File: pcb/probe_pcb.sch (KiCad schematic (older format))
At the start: 42 parts

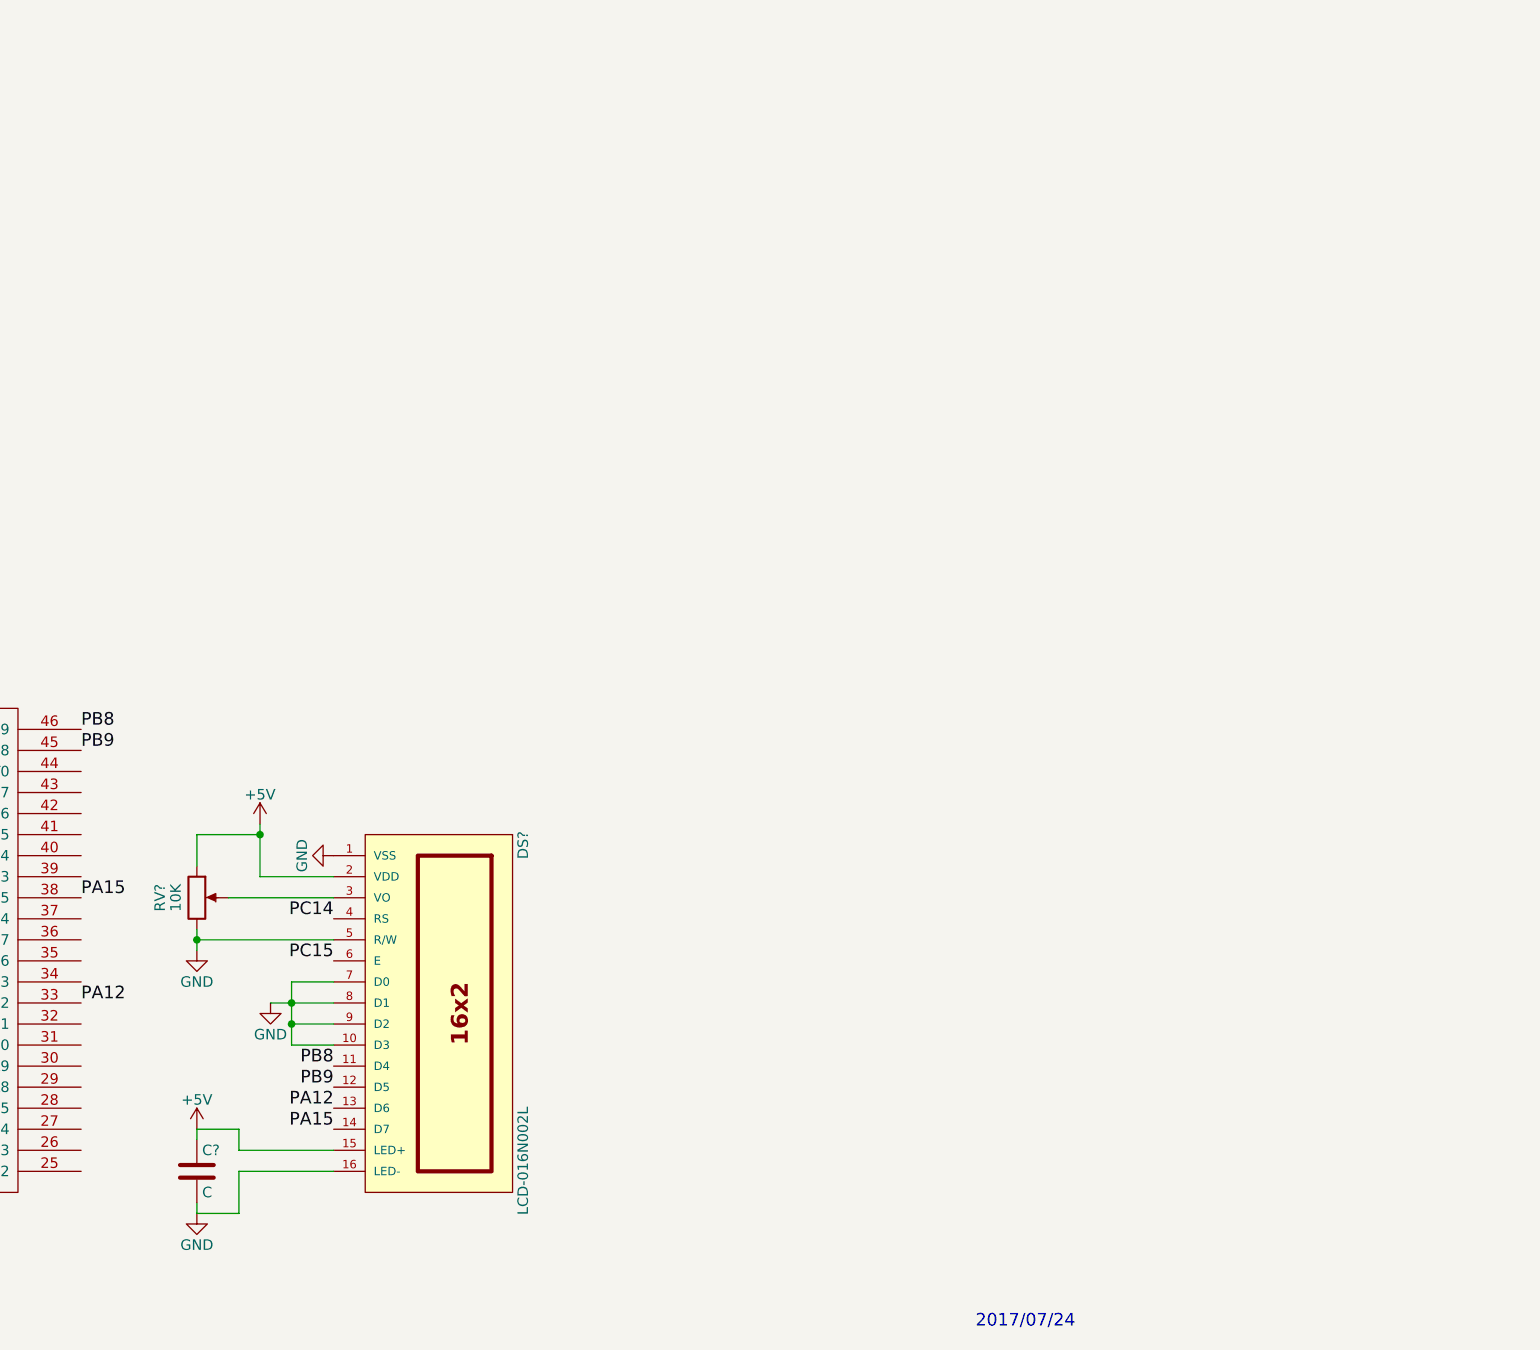
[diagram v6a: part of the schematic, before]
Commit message: Added ribbon cable connector for Pi, pi LCD
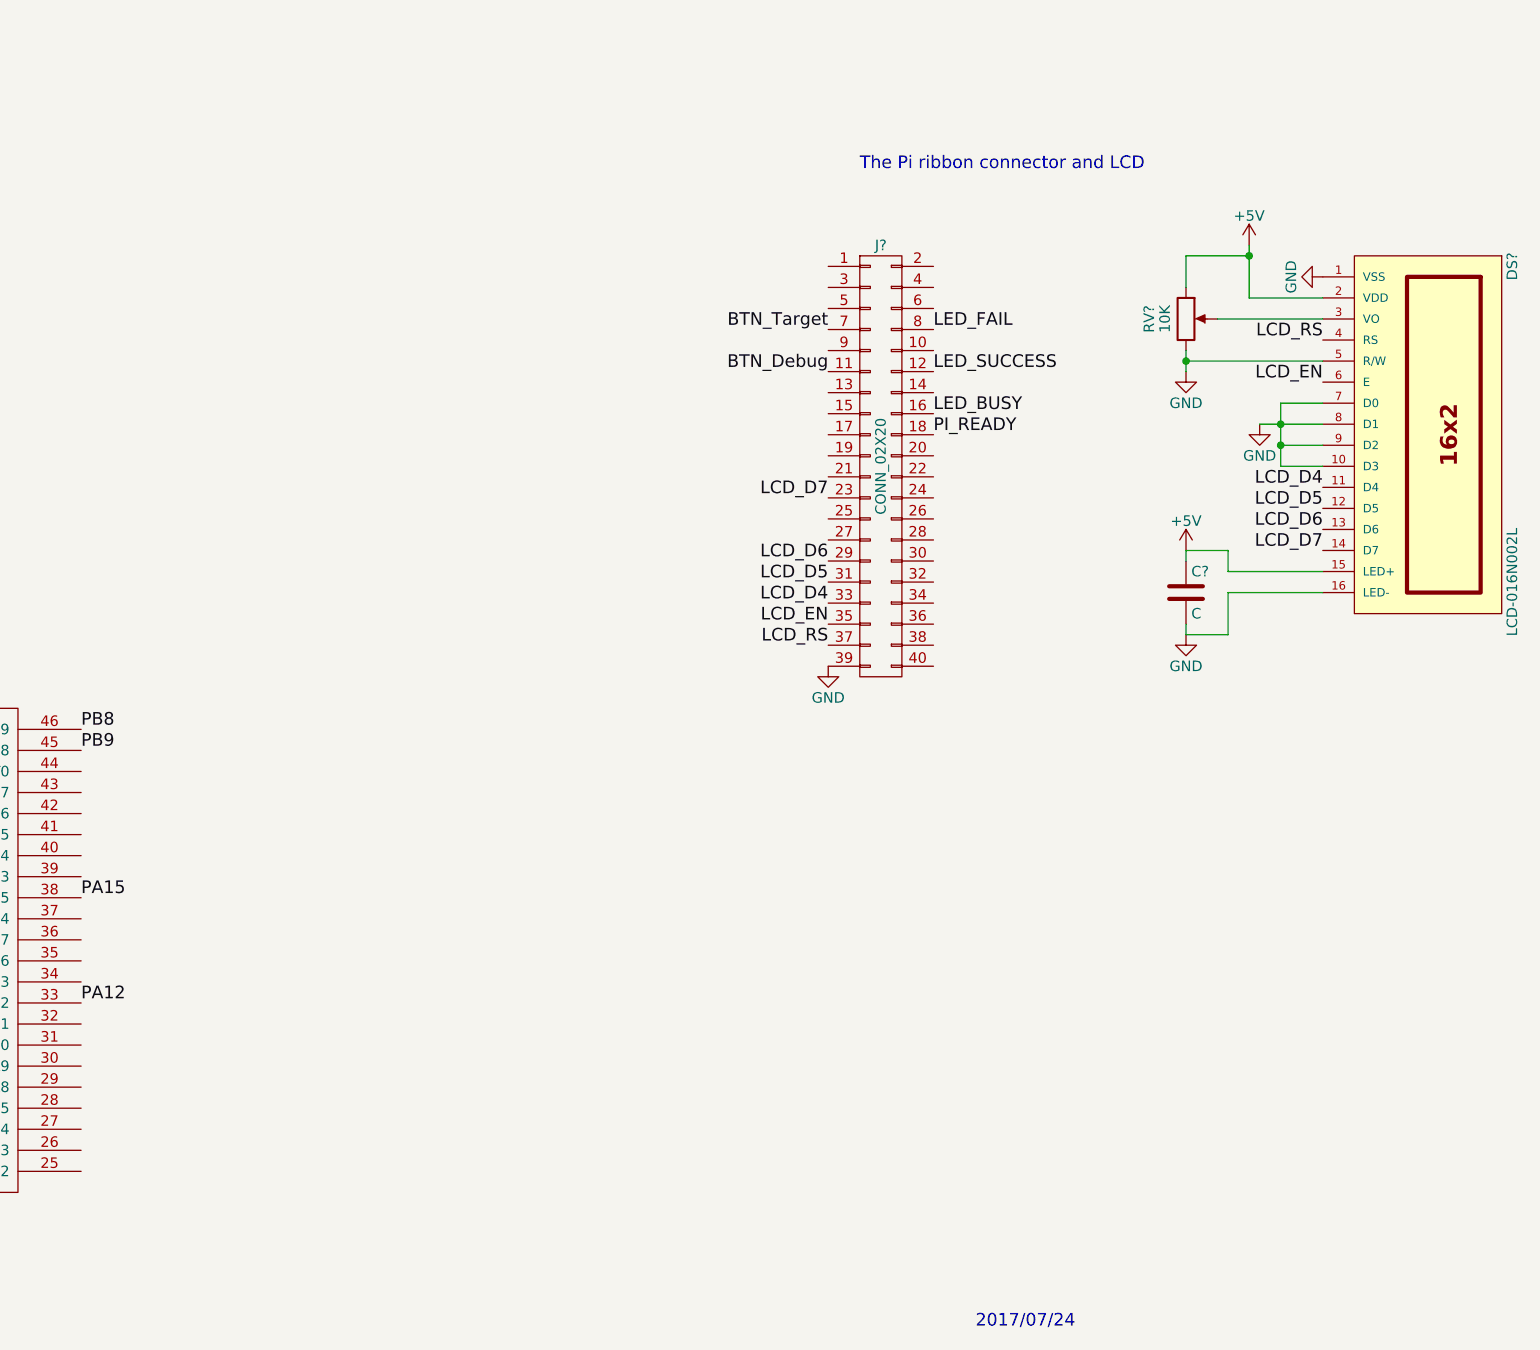
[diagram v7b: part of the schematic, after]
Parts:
- added J?: CONN_02X20, symbol CONN_02X20
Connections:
- net BTN_Debug: now also J?.11 (P11)
- net BTN_Target: now also J?.7 (P7)
- net GND: now also J?.39 (P39)
- net LED_BUSY: now also J?.16 (P16)
- net LED_FAIL: now also J?.8 (P8)
- net LED_SUCCESS: now also J?.12 (P12)
- net PA12: no longer DS?.13 (D6)
- net PA15: no longer DS?.14 (D7)
- net PB8: no longer DS?.11 (D4)
- net PB9: no longer DS?.12 (D5)
- net PC14: no longer DS?.4 (RS)
- net PC15: no longer DS?.6 (E)
- net PI_READY: now also J?.18 (P18)
- new net LCD_D4: DS?.11 (D4), J?.33 (P33)
- new net LCD_D5: DS?.12 (D5), J?.31 (P31)
- new net LCD_D6: DS?.13 (D6), J?.29 (P29)
- new net LCD_D7: DS?.14 (D7), J?.23 (P23)
- new net LCD_EN: DS?.6 (E), J?.35 (P35)
- new net LCD_RS: DS?.4 (RS), J?.37 (P37)
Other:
- note added: "The Pi ribbon connector and LCD"
- moved on the sheet: C?, DS?, RV?
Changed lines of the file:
@@
 LIBS:valves
 LIBS:stm_jig_lib
+LIBS:raspberrypi-gpio-cache
 LIBS:probe_pcb-cache
 EELAYER 25 0
@@
 L LCD-016N002L DS?
 U 1 1 5975A4A1
-P 10500 9550
-F 0 "DS?" H 9700 9950 50  0000 C CNN
-F 1 "LCD-016N002L" H 11200 9950 50  0000 C CNN
-F 2 "WC1602A" H 10500 9500 50  0001 C CIN
-F 3 "" H 10500 9550 50  0001 C CNN
-	1    10500 9550
+P 15200 6800
+F 0 "DS?" H 14400 7200 50  0000 C CNN
+F 1 "LCD-016N002L" H 15900 7200 50  0000 C CNN
+F 2 "WC1602A" H 15200 6750 50  0001 C CIN
+F 3 "" H 15200 6800 50  0001 C CNN
+	1    15200 6800
 	0    1    1    0
 $EndComp
@@
 Text Label 6900 8550 2    60   ~ 0
 PC15
-Text Label 10000 9100 2    60   ~ 0
-PC14
-Text Label 10000 9300 2    60   ~ 0
-PC15
 Text Label 8800 8200 0    60   ~ 0
 PB8
 Text Label 8800 8300 0    60   ~ 0
-PB9
-Text Label 10000 9800 2    60   ~ 0
-PB8
-Text Label 10000 9900 2    60   ~ 0
 PB9
 Text Label 8800 9500 0    60   ~ 0
@@
 Text Label 8800 9000 0    60   ~ 0
 PA15
-Text Label 10000 10100 2    60   ~ 0
-PA15
-Text Label 10000 10000 2    60   ~ 0
-PA12
-Wire Wire Line
-	10000 8900 9650 8900
-Wire Wire Line
-	9650 8900 9650 8650
+Wire Wire Line
+	14700 6150 14350 6150
+Wire Wire Line
+	14350 6150 14350 5900
 $Comp
 L +5V #PWR?
 U 1 1 59761C03
-P 9650 8650
-F 0 "#PWR?" H 9650 8500 50  0001 C CNN
-F 1 "+5V" H 9650 8790 50  0000 C CNN
-F 2 "" H 9650 8650 50  0001 C CNN
-F 3 "" H 9650 8650 50  0001 C CNN
-	1    9650 8650
+P 14350 5900
+F 0 "#PWR?" H 14350 5750 50  0001 C CNN
+F 1 "+5V" H 14350 6040 50  0000 C CNN
+F 2 "" H 14350 5900 50  0001 C CNN
+F 3 "" H 14350 5900 50  0001 C CNN
+	1    14350 5900
 	1    0    0    -1
 $EndComp
@@
 L POT RV?
 U 1 1 59761CDF
-P 9350 9000
-F 0 "RV?" V 9175 9000 50  0000 C CNN
-F 1 "10K" V 9250 9000 50  0000 C CNN
-F 2 "" H 9350 9000 50  0001 C CNN
-F 3 "" H 9350 9000 50  0001 C CNN
-	1    9350 9000
-	1    0    0    -1
-$EndComp
-Wire Wire Line
-	9500 9000 10000 9000
-Wire Wire Line
-	9350 8850 9350 8700
-Wire Wire Line
-	9350 8700 9650 8700
-Connection ~ 9650 8700
+P 14050 6250
+F 0 "RV?" V 13875 6250 50  0000 C CNN
+F 1 "10K" V 13950 6250 50  0000 C CNN
+F 2 "" H 14050 6250 50  0001 C CNN
+F 3 "" H 14050 6250 50  0001 C CNN
+	1    14050 6250
+	1    0    0    -1
+$EndComp
+Wire Wire Line
+	14200 6250 14700 6250
+Wire Wire Line
+	14050 6100 14050 5950
+Wire Wire Line
+	14050 5950 14350 5950
+Connection ~ 14350 5950
 $Comp
 L GND #PWR?
 U 1 1 59761E45
-P 9350 9250
-F 0 "#PWR?" H 9350 9000 50  0001 C CNN
-F 1 "GND" H 9350 9100 50  0000 C CNN
-F 2 "" H 9350 9250 50  0001 C CNN
-F 3 "" H 9350 9250 50  0001 C CNN
-	1    9350 9250
-	1    0    0    -1
-$EndComp
-Wire Wire Line
-	9350 9150 9350 9250
-Wire Wire Line
-	10000 9200 9350 9200
-Connection ~ 9350 9200
+P 14050 6500
+F 0 "#PWR?" H 14050 6250 50  0001 C CNN
+F 1 "GND" H 14050 6350 50  0000 C CNN
+F 2 "" H 14050 6500 50  0001 C CNN
+F 3 "" H 14050 6500 50  0001 C CNN
+	1    14050 6500
+	1    0    0    -1
+$EndComp
+Wire Wire Line
+	14050 6400 14050 6500
+Wire Wire Line
+	14700 6450 14050 6450
+Connection ~ 14050 6450
 $Comp
 L GND #PWR?
 U 1 1 59761FC4
-P 10000 8800
-F 0 "#PWR?" H 10000 8550 50  0001 C CNN
-F 1 "GND" H 10000 8650 50  0000 C CNN
-F 2 "" H 10000 8800 50  0001 C CNN
-F 3 "" H 10000 8800 50  0001 C CNN
-	1    10000 8800
+P 14700 6050
+F 0 "#PWR?" H 14700 5800 50  0001 C CNN
+F 1 "GND" H 14700 5900 50  0000 C CNN
+F 2 "" H 14700 6050 50  0001 C CNN
+F 3 "" H 14700 6050 50  0001 C CNN
+	1    14700 6050
 	0    1    1    0
 $EndComp
@@
 L GND #PWR?
 U 1 1 59762012
-P 9700 9500
-F 0 "#PWR?" H 9700 9250 50  0001 C CNN
-F 1 "GND" H 9700 9350 50  0000 C CNN
-F 2 "" H 9700 9500 50  0001 C CNN
-F 3 "" H 9700 9500 50  0001 C CNN
-	1    9700 9500
-	1    0    0    -1
-$EndComp
-Wire Wire Line
-	9700 9500 10000 9500
-Wire Wire Line
-	10000 9600 9800 9600
-Wire Wire Line
-	9800 9400 9800 9700
-Connection ~ 9800 9500
-Wire Wire Line
-	9800 9700 10000 9700
-Connection ~ 9800 9600
-Wire Wire Line
-	10000 9400 9800 9400
+P 14400 6750
+F 0 "#PWR?" H 14400 6500 50  0001 C CNN
+F 1 "GND" H 14400 6600 50  0000 C CNN
+F 2 "" H 14400 6750 50  0001 C CNN
+F 3 "" H 14400 6750 50  0001 C CNN
+	1    14400 6750
+	1    0    0    -1
+$EndComp
+Wire Wire Line
+	14400 6750 14700 6750
+Wire Wire Line
+	14700 6850 14500 6850
+Wire Wire Line
+	14500 6650 14500 6950
+Connection ~ 14500 6750
+Wire Wire Line
+	14500 6950 14700 6950
+Connection ~ 14500 6850
+Wire Wire Line
+	14700 6650 14500 6650
 $Comp
 L GND #PWR?
 U 1 1 5976236D
-P 9350 10500
-F 0 "#PWR?" H 9350 10250 50  0001 C CNN
-F 1 "GND" H 9350 10350 50  0000 C CNN
-F 2 "" H 9350 10500 50  0001 C CNN
-F 3 "" H 9350 10500 50  0001 C CNN
-	1    9350 10500
+P 14050 7750
+F 0 "#PWR?" H 14050 7500 50  0001 C CNN
+F 1 "GND" H 14050 7600 50  0000 C CNN
+F 2 "" H 14050 7750 50  0001 C CNN
+F 3 "" H 14050 7750 50  0001 C CNN
+	1    14050 7750
 	1    0    0    -1
 $EndComp
@@
 L +5V #PWR?
 U 1 1 597623BB
-P 9350 10100
-F 0 "#PWR?" H 9350 9950 50  0001 C CNN
-F 1 "+5V" H 9350 10240 50  0000 C CNN
-F 2 "" H 9350 10100 50  0001 C CNN
-F 3 "" H 9350 10100 50  0001 C CNN
-	1    9350 10100
+P 14050 7350
+F 0 "#PWR?" H 14050 7200 50  0001 C CNN
+F 1 "+5V" H 14050 7490 50  0000 C CNN
+F 2 "" H 14050 7350 50  0001 C CNN
+F 3 "" H 14050 7350 50  0001 C CNN
+	1    14050 7350
 	1    0    0    -1
 $EndComp
@@
 L C C?
 U 1 1 59762426
-P 9350 10300
-F 0 "C?" H 9375 10400 50  0000 L CNN
-F 1 "C" H 9375 10200 50  0000 L CNN
-F 2 "" H 9388 10150 50  0001 C CNN
-F 3 "" H 9350 10300 50  0001 C CNN
-	1    9350 10300
-	1    0    0    -1
-$EndComp
-Wire Wire Line
-	9350 10100 9350 10150
-Wire Wire Line
-	9350 10450 9350 10500
-Wire Wire Line
-	10000 10200 9550 10200
-Wire Wire Line
-	9550 10200 9550 10100
-Wire Wire Line
-	9550 10100 9350 10100
-Wire Wire Line
-	10000 10300 9550 10300
-Wire Wire Line
-	9550 10300 9550 10500
-Wire Wire Line
-	9550 10500 9350 10500
+P 14050 7550
+F 0 "C?" H 14075 7650 50  0000 L CNN
+F 1 "C" H 14075 7450 50  0000 L CNN
+F 2 "" H 14088 7400 50  0001 C CNN
+F 3 "" H 14050 7550 50  0001 C CNN
+	1    14050 7550
+	1    0    0    -1
+$EndComp
+Wire Wire Line
+	14050 7350 14050 7400
+Wire Wire Line
+	14050 7700 14050 7750
+Wire Wire Line
+	14700 7450 14250 7450
+Wire Wire Line
+	14250 7450 14250 7350
+Wire Wire Line
+	14250 7350 14050 7350
+Wire Wire Line
+	14700 7550 14250 7550
+Wire Wire Line
+	14250 7550 14250 7750
+Wire Wire Line
+	14250 7750 14050 7750
 $Comp
 L MMBT3904 Q?
@@
 Text Notes 13050 11050 0    60   ~ 0
 2017/07/24
+$Comp
+L CONN_02X20 J?
+U 1 1 59768D1C
+P 12600 6950
+F 0 "J?" H 12600 8000 50  0000 C CNN
+F 1 "CONN_02X20" V 12600 6950 50  0000 C CNN
+F 2 "" H 12600 6000 50  0001 C CNN
+F 3 "" H 12600 6000 50  0001 C CNN
+	1    12600 6950
+	1    0    0    -1
+$EndComp
+Text Label 14700 7050 2    60   ~ 0
+LCD_D4
+Text Label 14700 7150 2    60   ~ 0
+LCD_D5
+Text Label 14700 7250 2    60   ~ 0
+LCD_D6
+Text Label 14700 7350 2    60   ~ 0
+LCD_D7
+Text Label 14700 6550 2    60   ~ 0
+LCD_EN
+Text Label 14700 6350 2    60   ~ 0
+LCD_RS
+Text Label 12350 7700 2    60   ~ 0
+LCD_EN
+Text Label 12350 7400 2    60   ~ 0
+LCD_D6
+Text Label 12350 7500 2    60   ~ 0
+LCD_D5
+Text Label 12350 7600 2    60   ~ 0
+LCD_D4
+Text Label 12350 7100 2    60   ~ 0
+LCD_D7
+$Comp
+L GND #PWR?
+U 1 1 59769D17
+P 12350 7900
+F 0 "#PWR?" H 12350 7650 50  0001 C CNN
+F 1 "GND" H 12350 7750 50  0000 C CNN
+F 2 "" H 12350 7900 50  0001 C CNN
+F 3 "" H 12350 7900 50  0001 C CNN
+	1    12350 7900
+	1    0    0    -1
+$EndComp
+Text Label 12350 7800 2    60   ~ 0
+LCD_RS
+Text Label 12350 6300 2    60   ~ 0
+BTN_Target
+Text Label 12350 6500 2    60   ~ 0
+BTN_Debug
+Text Label 12850 6700 0    60   ~ 0
+LED_BUSY
+Text Label 12850 6500 0    60   ~ 0
+LED_SUCCESS
+Text Label 12850 6300 0    60   ~ 0
+LED_FAIL
+Text Label 12850 6800 0    60   ~ 0
+PI_READY
+Text Notes 12500 5550 0    60   ~ 0
+The Pi ribbon connector and LCD
 $EndSCHEMATC

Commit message: Now with two LCDs!
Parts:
- gave numbers to parts that had none: 43
